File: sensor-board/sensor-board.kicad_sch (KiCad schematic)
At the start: 54 parts, among them J1 USB_C_Receptacle_USB2.0_16P, J2 aux pwr, J3 SWD, J4 Conn_01x02, J5 Conn_01x02, Q1 Q_NMOS, U1 MLPF-WB55-01E3, U1 STM32WB55CCUx, U2 MCP1703Ax-300xxTT, U3 VL53L1CXV0FY1, Y1 32MHz, Y2 32.768

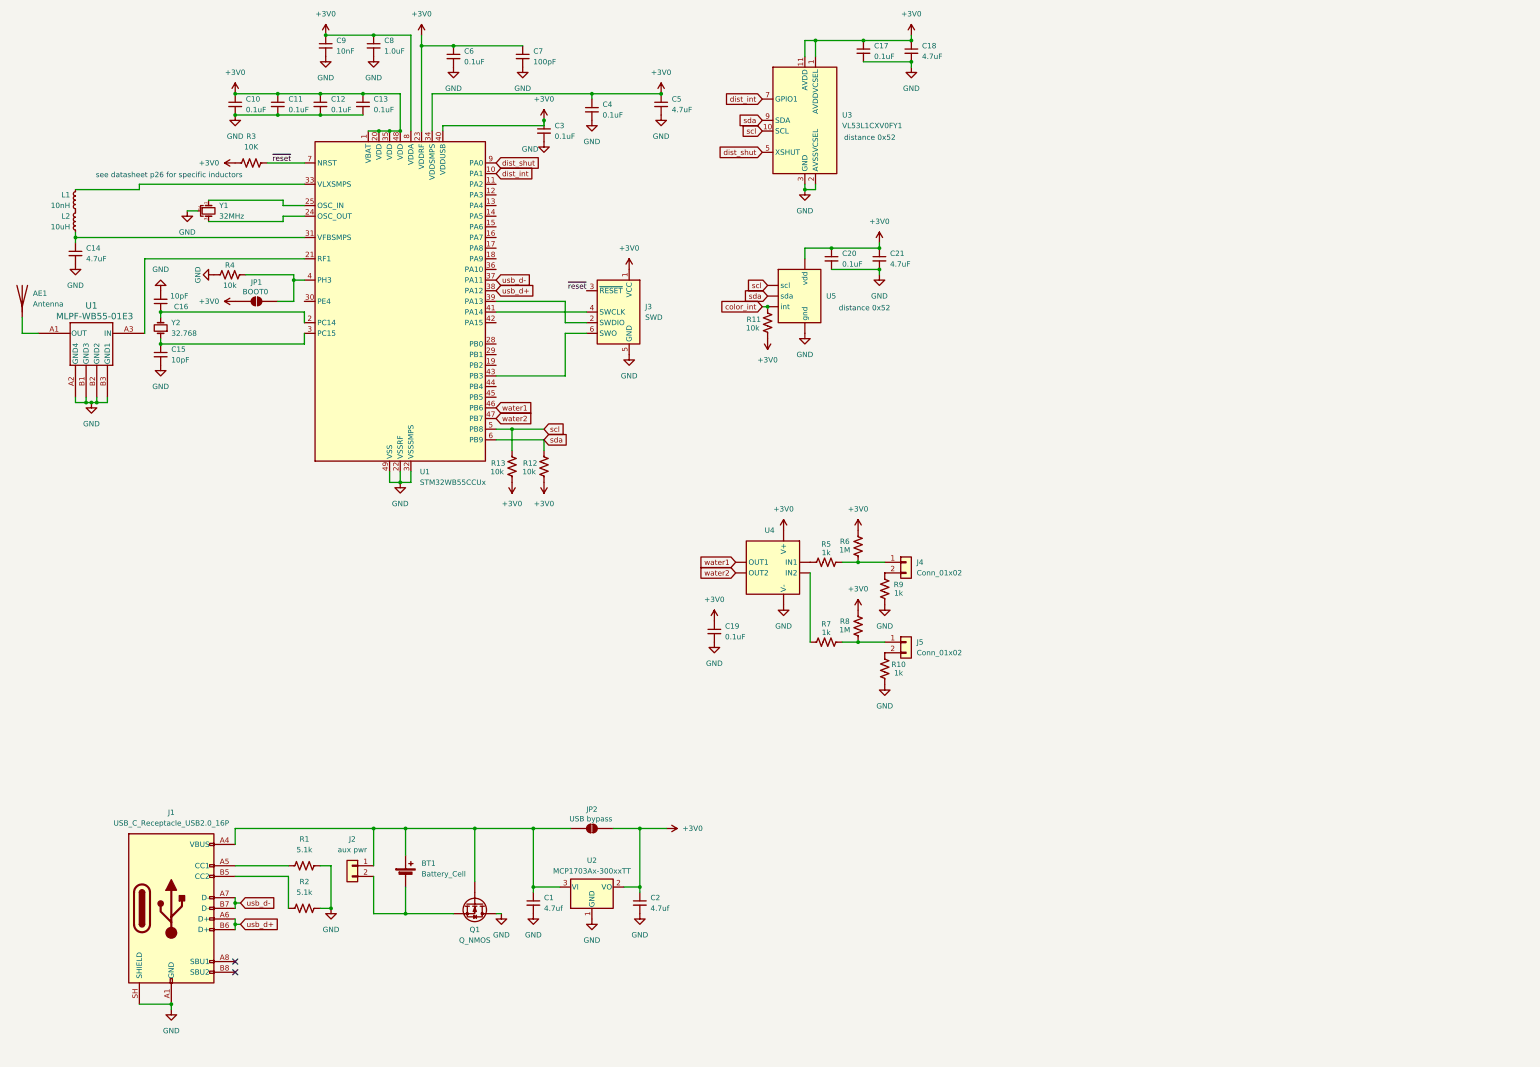
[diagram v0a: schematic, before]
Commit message: more or less final schematic; on to layout
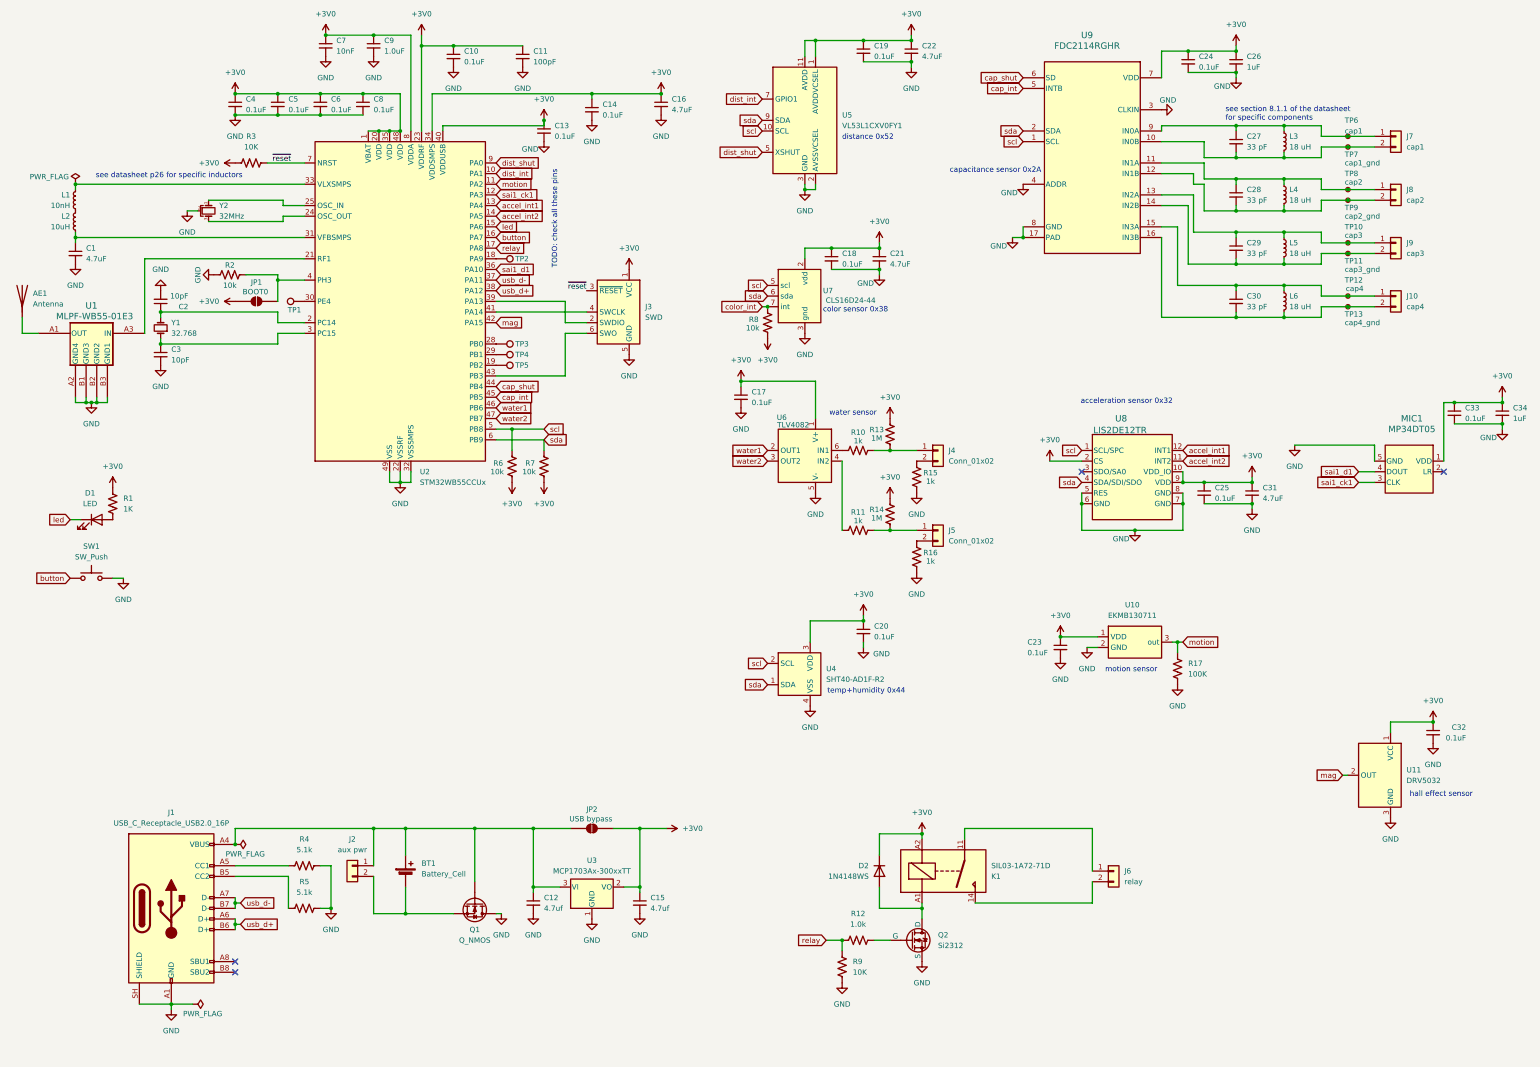
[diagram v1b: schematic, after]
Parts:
- added C20, C23, C24, C25, C32, C33: 0.1uF, symbol Device:C_Small
- added C26, C34: 1uF, symbol Device:C_Small
- added C27, C28, C29, C30: 33 pF, symbol Device:C_Small
- added C31: 4.7uF, symbol Device:C_Small
- added D1: LED, symbol Device:LED
- added D2: 1N4148WS, Diode_SMD:D_SOD-323, symbol Diode:1N4148WS
- added J10: cap4, symbol Connector_Generic:Conn_01x02
- added J6: relay, symbol Connector_Generic:Conn_01x02
- added J7: cap1, symbol Connector_Generic:Conn_01x02
- added J8: cap2, symbol Connector_Generic:Conn_01x02
- added J9: cap3, symbol Connector_Generic:Conn_01x02
- added K1: SIL03-1A72-71D, symbol Relay:Panasonic_ALFG2PF24
- added L3, L4, L5, L6: 18 uH, symbol Device:L_Small
- added MIC1: MP34DT05, vendor:HCLGA4_MP34_STM, symbol vendor:MP34DT05
- added Q2: Si2312, symbol Simulation_SPICE:NMOS
- added R1: 1K, symbol Device:R_US
- added R12: 1.0k, symbol Device:R_US
- added R17: 100K, symbol Device:R_US
- added R9: 10K, symbol Device:R_US
- added SW1: SW_Push, symbol Switch:SW_Push
- added TP1, TP2, TP3, TP4, TP5: TestPoint, symbol Connector:TestPoint
- added TP10: cap3, symbol Connector:TestPoint_Small
- added TP11: cap3_gnd, symbol Connector:TestPoint_Small
- added TP12: cap4, symbol Connector:TestPoint_Small
- added TP13: cap4_gnd, symbol Connector:TestPoint_Small
- added TP6: cap1, symbol Connector:TestPoint_Small
- added TP7: cap1_gnd, symbol Connector:TestPoint_Small
- added TP8: cap2, symbol Connector:TestPoint_Small
- added TP9: cap2_gnd, symbol Connector:TestPoint_Small
- added U10: EKMB130711, symbol vendor:EKMB1307113K
- added U11: DRV5032, Package_TO_SOT_SMD:SOT-23, symbol Sensor_Magnetic:DRV5033AJxDBZ
- added U4: SHT40-AD1F-R2, Sensor_Humidity:Sensirion_DFN-4_1.5x1.5mm_P0.8mm_SHT4x_NoCentralPad, symbol Sensor_Humidity:SHT4x
- added U8: LIS2DE12TR, vendor:LGA-12_STM, symbol vendor:LIS2DE12TR
- added U9: FDC2114RGHR, vendor:FDC2114RGHR, symbol vendor:FDC2114RGHR
- U6: renamed from U4; value (none) -> TLV4082; footprint (none) -> Package_TO_SOT_SMD:SOT-23-6
- U7: renamed from U5; value (none) -> CLS16D24-44
- renumbered C14 to C1, C6 to C10, C7 to C11, C1 to C12, C3 to C13, C4 to C14, C2 to C15, C5 to C16, C19 to C17, C20 to C18, C17 to C19, C16 to C2, C18 to C22, C15 to C3, C10 to C4, C11 to C5, C12 to C6, C9 to C7, C13 to C8, C8 to C9, R5 to R10, R7 to R11, R6 to R13, R8 to R14, R9 to R15, R10 to R16, R4 to R2, R1 to R4, R2 to R5, R13 to R6, R12 to R7, R11 to R8, U1 to U2, U2 to U3, U3 to U5, Y2 to Y1, Y1 to Y2
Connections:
- net +3V0: now also U6.1 (V+), U7.2 (vdd), C20.1, C23.1, C24.1, C25.1, C26.1, C31.1, C32.1, C33.1, C34.1, D2.1 (K), K1.A2, MIC1.1 (VDD), R1.1, U10.1 (VDD), U11.1 (VCC), U4.3 (VDD), U8.10 (VDD_IO), U8.2 (CS), U8.9 (VDD), U9.7 (VDD); no longer U6. (OUT2), U7. (gnd)
- net GND: now also U6.5 (V-), U7.3 (gnd), C20.2, C23.2, C24.2, C25.2, C26.2, C31.2, C32.2, C33.2, C34.2, MIC1.5 (GND), Q2.3 (S), R17.2, R9.1, SW1.2, U10.2 (GND), U11.3 (GND), U4.4 (VSS), U8.5 (RES), U8.6 (GND), U8.7 (GND), U8.8 (GND), U9.17 (PAD), U9.3 (CLKIN), U9.4 (ADDR), U9.8 (GND); no longer U6. (OUT2), U7. (gnd)
- net color_int: now also U7.7 (int); no longer U7. (gnd)
- net scl: now also U7.5 (scl), U4.2 (SCL), U8.1 (SCL/SPC), U9.1 (SCL); no longer U7. (gnd)
- net sda: now also U7.6 (sda), U4.1 (SDA), U8.4 (SDA/SDI/SDO), U9.2 (SDA); no longer U7. (gnd)
- net water1: now also U6.2 (OUT1); no longer U6. (OUT2)
- net water2: now also U6.3 (OUT2); no longer U6. (OUT2)
- net at R11.1: now also U6.4 (IN2); no longer U6. (OUT2)
- net at R10.1: now also U6.6 (IN1); no longer U6. (OUT2)
- net motion: now reaches U2.11 (PA2)
- net motion: now also R17.1, U10.3 (out)
- net sai1_ck1: now reaches U2.12 (PA3)
- net sai1_ck1: now also MIC1.3 (CLK)
- net accel_int1: now reaches U2.13 (PA4)
- net accel_int1: now also U8.12 (INT1)
- net accel_int2: now reaches U2.14 (PA5)
- net accel_int2: now also U8.11 (INT2)
- net led: now reaches U2.15 (PA6)
- net led: now also D1.1 (K)
- net button: now reaches U2.16 (PA7)
- net button: now also SW1.1
- net relay: now reaches U2.17 (PA8)
- net relay: now also R12.1, R9.2
- net at U2.18 (PA9): now also TP2.1
- net at U2.19 (PB2): now also TP5.1
- net at U2.28 (PB0): now also TP3.1
- net at U2.29 (PB1): now also TP4.1
- net at U2.30 (PE4): now also TP1.1
- net sai1_d1: now reaches U2.36 (PA10)
- net sai1_d1: now also MIC1.4 (DOUT)
- net mag: now reaches U2.42 (PA15)
- net mag: now also U11.2 (OUT)
- net cap_shut: now reaches U2.44 (PB4)
- net cap_shut: now also U9.6 (SD)
- net cap_int: now reaches U2.45 (PB5)
- net cap_int: now also U9.5 (INTB)
- new net: C29.1, J9.1 (Pin_1), L5.1, TP10.1, U9.13 (IN2A)
- new net: C29.2, J9.2 (Pin_2), L5.2, TP11.1, U9.14 (IN2B)
- new net: C27.2, J7.2 (Pin_2), L3.2, TP7.1, U9.10 (IN0B)
- new net: C30.1, J10.1 (Pin_1), L6.1, TP12.1, U9.15 (IN3A)
- new net: C28.1, J8.1 (Pin_1), L4.1, TP8.1, U9.11 (IN1A)
- new net: C28.2, J8.2 (Pin_2), L4.2, TP9.1, U9.12 (IN1B)
- new net: C30.2, J10.2 (Pin_2), L6.2, TP13.1, U9.16 (IN3B)
- new net: C27.1, J7.1 (Pin_1), L3.1, TP6.1, U9.9 (IN0A)
- new net: D2.2 (A), K1.A1, Q2.1 (D)
- new net: Q2.2 (G), R12.2
- new net: J6.1 (Pin_1), K1.11
- new net: J6.2 (Pin_2), K1.14
- new net: D1.2 (A), R1.2
- no-connect marks 2 -> 4
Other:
- note added: "TODO: check all these pins"
- note added: "acceleration sensor 0x32"
- note added: "capacitance sensor 0x2A"
- note added: "color sensor 0x38"
- note added: "hall effect sensor"
- note added: "motion sensor"
- note added: "see section 8.1.1 of the datasheet for specific components"
- note added: "temp+humidity 0x44"
- note added: "water sensor"
- title: (none) -> Sensor Board
- moved on the sheet: C17, J4, J5, R10, R11, R13, R14, R15, R16

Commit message: mostly footprint assignment, only not battery
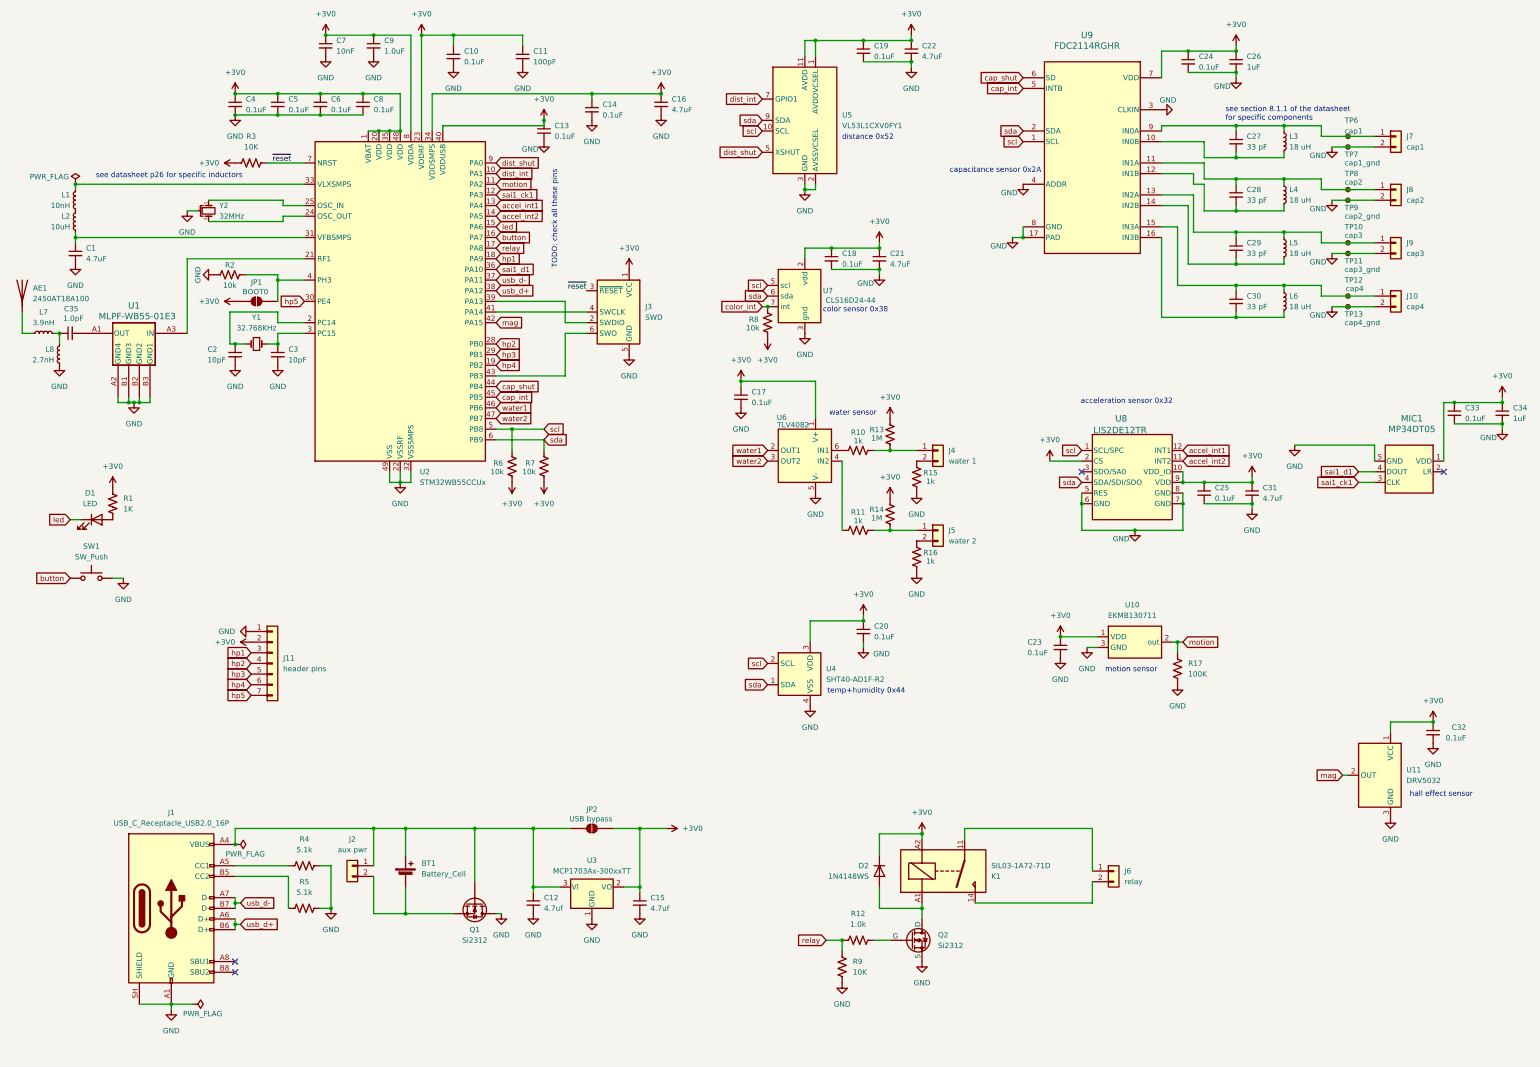
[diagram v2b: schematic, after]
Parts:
- removed TP1, TP2, TP3, TP4, TP5: TestPoint, symbol Connector:TestPoint
- added C35: 1.0pF, Capacitor_SMD:C_0402_1005Metric, symbol Device:C_Small
- added J11: header pins, Connector_PinHeader_2.54mm:PinHeader_1x07_P2.54mm_Vertical, symbol Connector_Generic:Conn_01x07
- added L7: 3.9nH, Inductor_SMD:L_0402_1005Metric, symbol Device:L_Small
- added L8: 2.7nH, Inductor_SMD:L_0402_1005Metric, symbol Device:L_Small
- AE1: value Antenna -> 2450AT18A100; footprint (none) -> vendor:XDCR_ACAG0801-2450-T
- C1, C10, C11, C12, C13, C14, C15, C16, C17, C18, C19, C2, C20, C21, C22, C23, C24, C25, C26, C27, C28, C29, C3, C30, C31, C32, C33, C34, C4, C5, C6, C7, C8, C9: footprint (none) -> Capacitor_SMD:C_0402_1005Metric
- D1: footprint (none) -> LED_SMD:LED_0805_2012Metric
- J1: footprint (none) -> Connector_USB:USB_C_Receptacle_G-Switch_GT-USB-7010ASV
- J10, J2, J6, J7, J8, J9: footprint (none) -> Connector_JST:JST_SH_BM02B-SRSS-TB_1x02-1MP_P1.00mm_Vertical
- J4: value Conn_01x02 -> water 1; footprint (none) -> Connector_JST:JST_SH_BM02B-SRSS-TB_1x02-1MP_P1.00mm_Vertical
- J5: value Conn_01x02 -> water 2; footprint (none) -> Connector_JST:JST_SH_BM02B-SRSS-TB_1x02-1MP_P1.00mm_Vertical
- JP1, JP2: footprint (none) -> Jumper:SolderJumper-2_P1.3mm_Open_RoundedPad1.0x1.5mm
- K1: footprint (none) -> vendor:SIL031A7271D
- L1: footprint (none) -> Inductor_SMD:L_0402_1005Metric
- L2: footprint (none) -> Inductor_SMD:L_0805_2012Metric
- L3, L4, L5, L6: footprint (none) -> Inductor_SMD:L_0603_1608Metric
- Q1: value Q_NMOS -> Si2312; footprint (none) -> Package_TO_SOT_SMD:SOT-23
- Q2: footprint (none) -> Package_TO_SOT_SMD:SOT-23
- R1, R10, R11, R12, R13, R14, R15, R16, R17, R2, R3, R4, R5, R6, R7, R8, R9: footprint (none) -> Resistor_SMD:R_0402_1005Metric
- SW1: footprint (none) -> Button_Switch_SMD:SW_SPST_TS-1088-xR020
- TP10, TP11, TP12, TP13, TP6, TP7, TP8, TP9: footprint (none) -> TestPoint:TestPoint_Pad_1.0x1.0mm
- U10: footprint (none) -> vendor:EKMB1307111K
- U7: footprint (none) -> vendor:CLS-16D24-44-DF8TR8
- Y1: value 32.768 -> 32.768KHz; footprint (none) -> Crystal:Crystal_SMD_3215-2Pin_3.2x1.5mm
- Y2: footprint (none) -> Crystal:Crystal_SMD_2016-4Pin_2.0x1.6mm
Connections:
- net +3V0: now also J11.2 (Pin_2)
- net GND: now also J10.2 (Pin_2), J7.2 (Pin_2), J8.2 (Pin_2), J9.2 (Pin_2), TP11.1, TP13.1, TP7.1, TP9.1, U10.3 (GND), J11.1 (Pin_1), L8.2; no longer U10.2 (GND)
- net motion: now also U10.2 (out); no longer U10.3 (out)
- net hp5: now reaches U2.30 (PE4)
- net hp5: now also J11.7 (Pin_7)
- net at C29.2, L5.2, U9.14 (IN2B): no longer J9.2 (Pin_2), TP11.1
- net at C27.2, L3.2, U9.10 (IN0B): no longer J7.2 (Pin_2), TP7.1
- net at C28.2, L4.2, U9.12 (IN1B): no longer J8.2 (Pin_2), TP9.1
- net at C30.2, L6.2, U9.16 (IN3B): no longer J10.2 (Pin_2), TP13.1
- net at U1.A1 (OUT): now also C35.2; no longer AE1.1 (A)
- net hp3: now reaches U2.29 (PB1)
- net hp3: now also J11.5 (Pin_5)
- net hp2: now reaches U2.28 (PB0)
- net hp2: now also J11.4 (Pin_4)
- net hp4: now reaches U2.19 (PB2)
- net hp4: now also J11.6 (Pin_6)
- net hp1: now reaches U2.18 (PA9)
- net hp1: now also J11.3 (Pin_3)
- new net: C35.1, L7.2, L8.1
- new net: AE1.1 (A), L7.1
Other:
- moved on the sheet: AE1, C2, C3, U1, Y1
